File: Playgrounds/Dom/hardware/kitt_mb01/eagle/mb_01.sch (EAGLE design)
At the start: 19 parts, among them IC1 LA5744TP

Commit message: Board and Library Updates  - kitt.con.lbr: connectors and connector references    -> DB01 Odometry Board Connector + board outline    -> Arduino Uno shield pins + (pin) overlay for ghostcar  - kitt.ic.lbr: added battery charger component from prev. board
 - mb01.*: motherboard for scaleauto
   -> added board connectors
   -> extended board size and corrected mounting holes
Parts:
- removed SJ2, SJ3: (no value), jumper:SJ
- added CON1: ARDUINO_UNO, kitt.con:ARDUINO_UNO
- added CON2: KITT.DB01, kitt.con:KITT.DB01
- added IC2: BQ24266RGET, kitt.ic:BQ24266RGET
- added REF4: REF_GC-BBV2.0, kitt.con:REF_GC-BBV2.0
- added SJ4, SJ5, SJ6: (no value), jumper:SJ
- added TP1, TP2: TPSQTP19SQ, testpad:TPSQTP19SQ
- L1.01: value (none) -> 22uH
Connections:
- net GND: now also CON1G$2.GND@1, CON1G$2.GND@2, CON2.GND@1, CON2.GND@2, CON2.GND@3, IC2PAD.THERMAL, IC2PINS.AGND, IC2PINS.PGND@2, SJ4.1, SJ5.1, SJ6.1; no longer SJ2.2, SJ3.2
- net GNDA: no longer SJ2.1, SJ3.1
- net N$4: now also TP1.TP
- net N$5: now also TP2.TP
- net THERM.1: now also SJ4.2, SJ5.2, SJ6.2

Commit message: entered the charging circuit
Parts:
- removed IC2: BQ24266RGET, kitt.ic:BQ24266RGET
- added C2.01: 1uF/16V, rcl:C-EUC0805
- added C2.02: 2.2uF/10V, rcl:C-EUC0805
- added C2.03, C2.04: 33nF/16V, rcl:C-EUC0805
- added IC2.00: BQ24266RGET, kitt.ic:BQ24266RGET
- added L1.02: 2.6uH, rcl:L-EUWE-TPC
- added L2.02: BEAD, inductor-neosid:SM-B5
- added LED1: LG_T679-E1F1-1, led:LG_T679-E1F1-1
- added Q1: (no value), transistor-power:P-MOSFET-SO8
- added R2: 10kR, rcl:R-EU_M0805
- added R2.01, R2.10, R2.11, R2.12, R2.13, R2.14, R2.15: 10kR, rcl:R-EU_R0603
- added R2.02: 31k6R, rcl:R-EU_R0603
- added R2.03: 1k62R, rcl:R-EU_R0603
- added R2.04: 5k62R, rcl:R-EU_R0603
- added R2.05: 11k8R, rcl:R-EU_R0603
- added R2.06: 10kR/NTC, ptc-ntc:V642
- added R2.07: 0R, rcl:R-EU_R0603
- added R3: 2k2R, rcl:R-EU_M0805
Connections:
- new net +4.1V: L2.02.2, R2.04.1, R2.10.2, R2.12.2, R2.14.2
- new net IC2.0.!CHG: IC2.00PINS.!CHG
- new net IC2.0.!PG: IC2.00PINS.!PG
- new net N$10: LED1.C, R2.1
- new net N$11: IC2.00PINS.VDPM, R2.01.2, R2.02.1
- new net N$12: C2.03.1, IC2.00PINS.SW@1, IC2.00PINS.SW@2, L1.02.2
- new net N$13: C2.03.2, IC2.00PINS.BOOT
- new net N$14: IC2.00PINS.BGATE, Q1.G
- new net N$15: IC2.00PINS.TS, R2.04.2, R2.05.1, R2.06.2
- new net N$16: L2.02.1, R2.07.1
- new net N$17: IC2.00PINS.BAT@1, IC2.00PINS.BAT@2, Q1.D
- new net N$18: C2.04.1, IC2.00PINS.SYS@1, IC2.00PINS.SYS@2, L1.02.1, Q1.S, R2.07.2
- new net N$19: IC2.00PINS.ISET, R2.03.2
- new net N$20: IC2.00PINS.IUSB@1, R2.10.1, R2.11.2
- new net N$21: IC2.00PINS.IUSB@2, R2.12.1, R2.13.2
- new net N$22: IC2.00PINS.IUSB@3, R2.14.1, R2.15.2
- new net N$8: C2.01.1, IC2.00PINS.PMID
- new net N$9: IC2.00PINS.IN@1, IC2.00PINS.IN@2, R2.02.2
- new net RAILS.RX: CON1G$3.IO.0, R2.2, R3.1
- new net V+: C2.02.1, IC2.00PINS.DRV
- net GND: now also C2.01.2, C2.02.2, C2.04.2, IC2.00PAD.THERMAL, IC2.00PINS.AGND, IC2.00PINS.PGND@1, IC2.00PINS.PGND@2, R2.01.1, R2.03.1, R2.05.2, R2.06.1, R2.11.1, R2.13.1, R2.15.1, R3.2; no longer IC2PAD.THERMAL, IC2PINS.AGND, IC2PINS.PGND@2
- net VCC/2: now also LED1.A
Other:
- note added: "D.Hoeglinger"
- note added: "KITT MB01 - Battery Charger"
- note added: "KITT MB01 - Connectors"
- note added: "The LED here is dual purpose: 1. Idicator for Rail Voltage 2. Reverse Polarity Protection for the SoC Board RX independent from the main power chain"

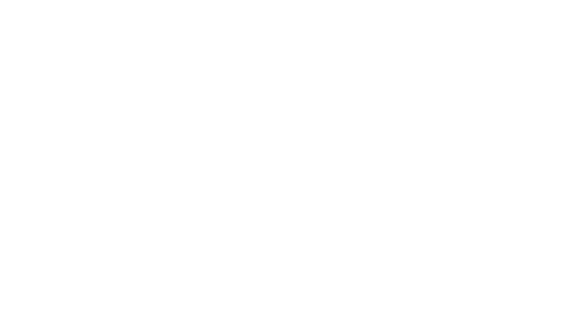
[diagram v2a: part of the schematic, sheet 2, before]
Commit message: started copying the layout surrounding the battery charger from the previous version imported bottom copper reference seems to be not quite to scale, but no worries
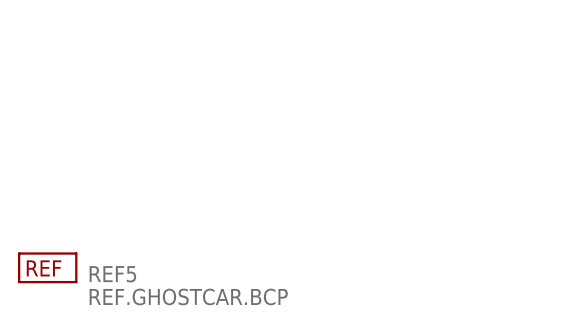
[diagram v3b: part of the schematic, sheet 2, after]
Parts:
- added REF5: REF.GHOSTCAR.BCP, kitt.refs:REF.GHOSTCAR.BCP
- R2.01, R2.02, R2.03, R2.04, R2.05, R2.07, R2.10, R2.11, R2.12, R2.13, R2.14, R2.15: device rcl:R-EU_R0603 -> rcl:R-EU_R0402
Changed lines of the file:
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@@
 <part name="C2.01" library="rcl" deviceset="C-EU" device="C0805" value="1uF/16V"/>
 <part name="GND9" library="supply1" deviceset="GND" device=""/>
-<part name="R2.01" library="rcl" deviceset="R-EU_" device="R0603" value="10kR"/>
-<part name="R2.02" library="rcl" deviceset="R-EU_" device="R0603" value="31k6R"/>
+<part name="R2.01" library="rcl" deviceset="R-EU_" device="R0402" value="10kR"/>
+<part name="R2.02" library="rcl" deviceset="R-EU_" device="R0402" value="31k6R"/>
 <part name="GND10" library="supply1" deviceset="GND" device=""/>
 <part name="P+U1" library="supply1" deviceset="V+" device="" value="VDRV"/>
@@
 <part name="Q1" library="transistor-power" deviceset="P-MOSFET-SO8" device=""/>
 <part name="SUPPLY1" library="supply2" deviceset="+4.1V" device="" value="VBAT+4.1V"/>
-<part name="R2.03" library="rcl" deviceset="R-EU_" device="R0603" value="1k62R"/>
-<part name="R2.04" library="rcl" deviceset="R-EU_" device="R0603" value="5k62R"/>
-<part name="R2.05" library="rcl" deviceset="R-EU_" device="R0603" value="11k8R"/>
+<part name="R2.03" library="rcl" deviceset="R-EU_" device="R0402" value="1k62R"/>
+<part name="R2.04" library="rcl" deviceset="R-EU_" device="R0402" value="5k62R"/>
+<part name="R2.05" library="rcl" deviceset="R-EU_" device="R0402" value="11k8R"/>
 <part name="R2.06" library="ptc-ntc" deviceset="V642" device="" value="10kR/NTC"/>
 <part name="GND12" library="supply1" deviceset="GND" device=""/>
@@
 <part name="GND13" library="supply1" deviceset="GND" device=""/>
 <part name="L2.02" library="inductor-neosid" deviceset="SM-B" device="5" value="BEAD"/>
-<part name="R2.07" library="rcl" deviceset="R-EU_" device="R0603" value="0R"/>
+<part name="R2.07" library="rcl" deviceset="R-EU_" device="R0402" value="0R"/>
 <part name="GND14" library="supply1" deviceset="GND" device=""/>
-<part name="R2.10" library="rcl" deviceset="R-EU_" device="R0603" value="10kR"/>
-<part name="R2.11" library="rcl" deviceset="R-EU_" device="R0603" value="10kR"/>
-<part name="R2.12" library="rcl" deviceset="R-EU_" device="R0603" value="10kR"/>
-<part name="R2.13" library="rcl" deviceset="R-EU_" device="R0603" value="10kR"/>
-<part name="R2.14" library="rcl" deviceset="R-EU_" device="R0603" value="10kR"/>
-<part name="R2.15" library="rcl" deviceset="R-EU_" device="R0603" value="10kR"/>
+<part name="R2.10" library="rcl" deviceset="R-EU_" device="R0402" value="10kR"/>
+<part name="R2.11" library="rcl" deviceset="R-EU_" device="R0402" value="10kR"/>
+<part name="R2.12" library="rcl" deviceset="R-EU_" device="R0402" value="10kR"/>
+<part name="R2.13" library="rcl" deviceset="R-EU_" device="R0402" value="10kR"/>
+<part name="R2.14" library="rcl" deviceset="R-EU_" device="R0402" value="10kR"/>
+<part name="R2.15" library="rcl" deviceset="R-EU_" device="R0402" value="10kR"/>
 <part name="SUPPLY3" library="supply2" deviceset="+4.1V" device="" value="VBAT+4.1V"/>
 <part name="GND15" library="supply1" deviceset="GND" device=""/>
+<part name="REF5" library="kitt.refs" deviceset="REF.GHOSTCAR.BCP" device=""/>
 </parts>
 <sheets>
@@
 <instance part="SUPPLY3" gate="P" x="157.48" y="86.36"/>
 <instance part="GND15" gate="1" x="177.8" y="40.64"/>
+<instance part="REF5" gate="G$1" x="7.62" y="15.24"/>
 </instances>
 <busses>

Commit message: did some more work on copying the charger layout
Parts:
- added C2.05: 22uF, rcl:CPOL-EUA/3216-18R
- C2.03: device rcl:C-EUC0805 -> rcl:C-EUC0603
- L2.02: device inductor-neosid:SM-B5 -> rcl:L-EUL2012C
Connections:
- removed net N$17: IC2.00PINS.BAT@1, IC2.00PINS.BAT@2, Q1.D
- net +4.1V: now also C2.05.+, IC2.00PINS.BAT@1, IC2.00PINS.BAT@2, Q1.D
- net GND: now also C2.05.-
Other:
- moved on the sheet: R2.04, R2.05, R2.06
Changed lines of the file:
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@@
 <part name="GND11" library="supply1" deviceset="GND" device=""/>
 <part name="L1.02" library="rcl" deviceset="L-EU" device="WE-TPC" value="2.6uH"/>
-<part name="C2.03" library="rcl" deviceset="C-EU" device="C0805" value="33nF/16V"/>
+<part name="C2.03" library="rcl" deviceset="C-EU" device="C0603" value="33nF/16V"/>
 <part name="Q1" library="transistor-power" deviceset="P-MOSFET-SO8" device=""/>
 <part name="SUPPLY1" library="supply2" deviceset="+4.1V" device="" value="VBAT+4.1V"/>
@@
 <part name="C2.04" library="rcl" deviceset="C-EU" device="C0805" value="33nF/16V"/>
 <part name="GND13" library="supply1" deviceset="GND" device=""/>
-<part name="L2.02" library="inductor-neosid" deviceset="SM-B" device="5" value="BEAD"/>
+<part name="L2.02" library="rcl" deviceset="L-EU" device="L2012C" value="BEAD"/>
 <part name="R2.07" library="rcl" deviceset="R-EU_" device="R0402" value="0R"/>
 <part name="GND14" library="supply1" deviceset="GND" device=""/>
@@
 <part name="GND15" library="supply1" deviceset="GND" device=""/>
 <part name="REF5" library="kitt.refs" deviceset="REF.GHOSTCAR.BCP" device=""/>
+<part name="C2.05" library="rcl" deviceset="CPOL-EU" device="A/3216-18R" value="22uF"/>
+<part name="GND16" library="supply1" deviceset="GND" device=""/>
+<part name="SUPPLY4" library="supply2" deviceset="+4.1V" device="" value="VBAT+4.1V"/>
 </parts>
 <sheets>
@@
 <instance part="SUPPLY1" gate="P" x="220.98" y="147.32"/>
 <instance part="R2.03" gate="G$1" x="147.32" y="96.52" rot="MR0"/>
-<instance part="R2.04" gate="G$1" x="185.42" y="109.22" rot="MR270"/>
-<instance part="R2.05" gate="G$1" x="185.42" y="96.52" rot="MR270"/>
-<instance part="R2.06" gate="1" x="195.58" y="96.52"/>
-<instance part="GND12" gate="1" x="195.58" y="83.82"/>
-<instance part="SUPPLY2" gate="P" x="185.42" y="119.38"/>
+<instance part="R2.04" gate="G$1" x="195.58" y="73.66" rot="MR270"/>
+<instance part="R2.05" gate="G$1" x="195.58" y="53.34" rot="MR270"/>
+<instance part="R2.06" gate="1" x="205.74" y="53.34"/>
+<instance part="GND12" gate="1" x="205.74" y="40.64"/>
+<instance part="SUPPLY2" gate="P" x="195.58" y="83.82"/>
 <instance part="C2.04" gate="G$1" x="185.42" y="137.16"/>
 <instance part="GND13" gate="1" x="185.42" y="129.54"/>
@@
 <instance part="GND15" gate="1" x="177.8" y="40.64"/>
 <instance part="REF5" gate="G$1" x="7.62" y="15.24"/>
+<instance part="C2.05" gate="G$1" x="220.98" y="104.14"/>
+<instance part="GND16" gate="1" x="220.98" y="91.44"/>
+<instance part="SUPPLY4" gate="P" x="220.98" y="121.92"/>
 </instances>
 <busses>
@@
 <segment>
 <pinref part="R2.05" gate="G$1" pin="2"/>
-<wire x1="185.42" y1="91.44" x2="185.42" y2="88.9" width="0.1524" layer="91"/>
-<wire x1="185.42" y1="88.9" x2="195.58" y2="88.9" width="0.1524" layer="91"/>
+<wire x1="195.58" y1="48.26" x2="195.58" y2="45.72" width="0.1524" layer="91"/>
+<wire x1="195.58" y1="45.72" x2="205.74" y2="45.72" width="0.1524" layer="91"/>
 <pinref part="GND12" gate="1" pin="GND"/>
-<wire x1="195.58" y1="88.9" x2="195.58" y2="86.36" width="0.1524" layer="91"/>
+<wire x1="205.74" y1="45.72" x2="205.74" y2="43.18" width="0.1524" layer="91"/>
 <pinref part="R2.06" gate="1" pin="1"/>
-<wire x1="195.58" y1="91.44" x2="195.58" y2="88.9" width="0.1524" layer="91"/>
-<junction x="195.58" y="88.9"/>
+<wire x1="205.74" y1="48.26" x2="205.74" y2="45.72" width="0.1524" layer="91"/>
+<junction x="205.74" y="45.72"/>
 </segment>
 <segment>
@@
 <junction x="167.64" y="45.72"/>
 </segment>
+<segment>
+<pinref part="C2.05" gate="G$1" pin="-"/>
+<pinref part="GND16" gate="1" pin="GND"/>
+<wire x1="220.98" y1="93.98" x2="220.98" y2="99.06" width="0.1524" layer="91"/>
+</segment>
 </net>
 <net name="N$8" class="0">
@@
 </segment>
 </net>
-<net name="N$17" class="0">
-<segment>
-<pinref part="Q1" gate="G$1" pin="D"/>
-<pinref part="IC2.00" gate="PINS" pin="BAT@2"/>
-<wire x1="175.26" y1="114.3" x2="175.26" y2="111.76" width="0.1524" layer="91"/>
-<wire x1="175.26" y1="111.76" x2="144.78" y2="111.76" width="0.1524" layer="91"/>
-<pinref part="IC2.00" gate="PINS" pin="BAT@1"/>
-<wire x1="144.78" y1="111.76" x2="139.7" y2="111.76" width="0.1524" layer="91"/>
-<wire x1="139.7" y1="114.3" x2="144.78" y2="114.3" width="0.1524" layer="91"/>
-<wire x1="144.78" y1="114.3" x2="144.78" y2="111.76" width="0.1524" layer="91"/>
-<junction x="144.78" y="111.76"/>
-</segment>
-</net>
 <net name="+4.1V" class="0">
 <segment>
 <pinref part="R2.04" gate="G$1" pin="1"/>
 <pinref part="SUPPLY2" gate="P" pin="+4.1V"/>
-<wire x1="185.42" y1="116.84" x2="185.42" y2="114.3" width="0.1524" layer="91"/>
+<wire x1="195.58" y1="81.28" x2="195.58" y2="78.74" width="0.1524" layer="91"/>
 </segment>
 <segment>
 <pinref part="L2.02" gate="G$1" pin="2"/>
 <pinref part="SUPPLY1" gate="P" pin="+4.1V"/>
-<wire x1="218.44" y1="142.24" x2="220.98" y2="142.24" width="0.1524" layer="91"/>
+<wire x1="215.9" y1="137.16" x2="220.98" y2="142.24" width="0.1524" layer="91"/>
 <wire x1="220.98" y1="142.24" x2="220.98" y2="144.78" width="0.1524" layer="91"/>
 </segment>
@@
 <junction x="167.64" y="81.28"/>
 </segment>
+<segment>
+<pinref part="Q1" gate="G$1" pin="D"/>
+<pinref part="IC2.00" gate="PINS" pin="BAT@2"/>
+<wire x1="175.26" y1="114.3" x2="175.26" y2="111.76" width="0.1524" layer="91"/>
+<wire x1="175.26" y1="111.76" x2="144.78" y2="111.76" width="0.1524" layer="91"/>
+<pinref part="IC2.00" gate="PINS" pin="BAT@1"/>
+<wire x1="144.78" y1="111.76" x2="139.7" y2="111.76" width="0.1524" layer="91"/>
+<wire x1="139.7" y1="114.3" x2="144.78" y2="114.3" width="0.1524" layer="91"/>
+<wire x1="144.78" y1="114.3" x2="144.78" y2="111.76" width="0.1524" layer="91"/>
+<junction x="144.78" y="111.76"/>
+<wire x1="175.26" y1="111.76" x2="220.98" y2="111.76" width="0.1524" layer="91"/>
+<junction x="175.26" y="111.76"/>
+<wire x1="220.98" y1="111.76" x2="220.98" y2="119.38" width="0.1524" layer="91"/>
+<pinref part="C2.05" gate="G$1" pin="+"/>
+<wire x1="220.98" y1="106.68" x2="220.98" y2="111.76" width="0.1524" layer="91"/>
+<junction x="220.98" y="111.76"/>
+<pinref part="SUPPLY4" gate="P" pin="+4.1V"/>
+</segment>
 </net>
 <net name="N$15" class="0">
@@
 <pinref part="R2.04" gate="G$1" pin="2"/>
 <wire x1="139.7" y1="104.14" x2="185.42" y2="104.14" width="0.1524" layer="91"/>
+<wire x1="185.42" y1="104.14" x2="185.42" y2="60.96" width="0.1524" layer="91"/>
 <pinref part="R2.05" gate="G$1" pin="1"/>
-<wire x1="185.42" y1="101.6" x2="185.42" y2="104.14" width="0.1524" layer="91"/>
-<junction x="185.42" y="104.14"/>
+<wire x1="195.58" y1="58.42" x2="195.58" y2="60.96" width="0.1524" layer="91"/>
 <pinref part="R2.06" gate="1" pin="2"/>
-<wire x1="185.42" y1="104.14" x2="195.58" y2="104.14" width="0.1524" layer="91"/>
-<wire x1="195.58" y1="104.14" x2="195.58" y2="101.6" width="0.1524" layer="91"/>
+<wire x1="195.58" y1="60.96" x2="195.58" y2="68.58" width="0.1524" layer="91"/>
+<wire x1="205.74" y1="60.96" x2="205.74" y2="58.42" width="0.1524" layer="91"/>
+<wire x1="185.42" y1="60.96" x2="195.58" y2="60.96" width="0.1524" layer="91"/>
+<junction x="195.58" y="60.96"/>
+<wire x1="195.58" y1="60.96" x2="205.74" y2="60.96" width="0.1524" layer="91"/>
 </segment>
 </net>
@@
 <pinref part="R2.07" gate="G$1" pin="1"/>
 <pinref part="L2.02" gate="G$1" pin="1"/>
-<wire x1="205.74" y1="142.24" x2="210.82" y2="142.24" width="0.1524" layer="91"/>
-</segment>
-</net>
+<wire x1="205.74" y1="142.24" x2="215.9" y2="147.32" width="0.1524" layer="91"/>
+</segment>
+</net>

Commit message: finished up on the charger circuit, roughly...
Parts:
- removed REF5: REF.GHOSTCAR.BCP, kitt.refs:REF.GHOSTCAR.BCP
- added R2.08: [10kR/NTC], rcl:R-EU_R0402
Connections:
- net +4.1V: now also R2.07.1; no longer L2.02.2
- net GND: now also R2.08.2
- net N$15: now also R2.08.1
- net N$16: now also L2.02.2, R2.07.2; no longer L2.02.1, R2.07.1
- net N$18: now also L2.02.1; no longer R2.07.2
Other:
- moved on the sheet: L2.02, R2.07
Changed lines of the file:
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@@
 <part name="SUPPLY3" library="supply2" deviceset="+4.1V" device="" value="VBAT+4.1V"/>
 <part name="GND15" library="supply1" deviceset="GND" device=""/>
-<part name="REF5" library="kitt.refs" deviceset="REF.GHOSTCAR.BCP" device=""/>
 <part name="C2.05" library="rcl" deviceset="CPOL-EU" device="A/3216-18R" value="22uF"/>
 <part name="GND16" library="supply1" deviceset="GND" device=""/>
 <part name="SUPPLY4" library="supply2" deviceset="+4.1V" device="" value="VBAT+4.1V"/>
+<part name="R2.08" library="rcl" deviceset="R-EU_" device="R0402" value="[10kR/NTC]"/>
 </parts>
 <sheets>
@@
 <instance part="C2.04" gate="G$1" x="185.42" y="137.16"/>
 <instance part="GND13" gate="1" x="185.42" y="129.54"/>
-<instance part="L2.02" gate="G$1" x="215.9" y="142.24"/>
-<instance part="R2.07" gate="G$1" x="200.66" y="142.24" rot="MR0"/>
+<instance part="L2.02" gate="G$1" x="200.66" y="142.24" rot="MR270"/>
+<instance part="R2.07" gate="G$1" x="213.36" y="142.24" rot="MR0"/>
 <instance part="GND14" gate="1" x="157.48" y="96.52" rot="R90"/>
 <instance part="R2.10" gate="G$1" x="157.48" y="73.66" rot="MR90"/>
@@
 <instance part="SUPPLY3" gate="P" x="157.48" y="86.36"/>
 <instance part="GND15" gate="1" x="177.8" y="40.64"/>
-<instance part="REF5" gate="G$1" x="7.62" y="15.24"/>
 <instance part="C2.05" gate="G$1" x="220.98" y="104.14"/>
 <instance part="GND16" gate="1" x="220.98" y="91.44"/>
 <instance part="SUPPLY4" gate="P" x="220.98" y="121.92"/>
+<instance part="R2.08" gate="G$1" x="223.52" y="53.34" rot="MR270"/>
 </instances>
 <busses>
@@
 <wire x1="205.74" y1="48.26" x2="205.74" y2="45.72" width="0.1524" layer="91"/>
 <junction x="205.74" y="45.72"/>
+<pinref part="R2.08" gate="G$1" pin="2"/>
+<wire x1="223.52" y1="48.26" x2="223.52" y2="45.72" width="0.1524" layer="91"/>
+<wire x1="223.52" y1="45.72" x2="205.74" y2="45.72" width="0.1524" layer="91"/>
 </segment>
 <segment>
@@
 </segment>
 <segment>
-<pinref part="L2.02" gate="G$1" pin="2"/>
 <pinref part="SUPPLY1" gate="P" pin="+4.1V"/>
-<wire x1="215.9" y1="137.16" x2="220.98" y2="142.24" width="0.1524" layer="91"/>
 <wire x1="220.98" y1="142.24" x2="220.98" y2="144.78" width="0.1524" layer="91"/>
+<pinref part="R2.07" gate="G$1" pin="1"/>
+<wire x1="218.44" y1="142.24" x2="220.98" y2="142.24" width="0.1524" layer="91"/>
 </segment>
 <segment>
@@
 <junction x="195.58" y="60.96"/>
 <wire x1="195.58" y1="60.96" x2="205.74" y2="60.96" width="0.1524" layer="91"/>
+<pinref part="R2.08" gate="G$1" pin="1"/>
+<wire x1="223.52" y1="58.42" x2="223.52" y2="60.96" width="0.1524" layer="91"/>
+<wire x1="223.52" y1="60.96" x2="205.74" y2="60.96" width="0.1524" layer="91"/>
+<junction x="205.74" y="60.96"/>
 </segment>
 </net>
@@
 <wire x1="185.42" y1="142.24" x2="185.42" y2="139.7" width="0.1524" layer="91"/>
 <junction x="175.26" y="142.24"/>
-<pinref part="R2.07" gate="G$1" pin="2"/>
-<wire x1="185.42" y1="142.24" x2="195.58" y2="142.24" width="0.1524" layer="91"/>
+<pinref part="L2.02" gate="G$1" pin="1"/>
+<wire x1="195.58" y1="142.24" x2="185.42" y2="142.24" width="0.1524" layer="91"/>
 <junction x="185.42" y="142.24"/>
-</segment>
-</net>
-<net name="N$16" class="0">
-<segment>
-<pinref part="R2.07" gate="G$1" pin="1"/>
-<pinref part="L2.02" gate="G$1" pin="1"/>
-<wire x1="205.74" y1="142.24" x2="215.9" y2="147.32" width="0.1524" layer="91"/>
 </segment>
 </net>
@@
 </segment>
 </net>
+<net name="N$16" class="0">
+<segment>
+<pinref part="L2.02" gate="G$1" pin="2"/>
+<pinref part="R2.07" gate="G$1" pin="2"/>
+<wire x1="205.74" y1="142.24" x2="208.28" y2="142.24" width="0.1524" layer="91"/>
+</segment>
+</net>
